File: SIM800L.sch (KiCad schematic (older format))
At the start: 9 parts, among them P3 CONN_01X06, P4 CONN_01X06, Q1 BC849

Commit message: Modifico algunos componentes. Seteo algunos encapsulados. Ordeno los componentes en el PCB.
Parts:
- D5: footprint (none) -> LEDs:LED_1206
- D6, D7: footprint (none) -> Diodes_SMD:SOD-123
- P3, P4: footprint (none) -> Pin_Headers:Pin_Header_Angled_1x06
- Q1: footprint SOT-23 -> TO_SOT_Packages_SMD:SOT-23
- R2, R3, R4: footprint (none) -> SMD_Packages:SMD-1206_Pol
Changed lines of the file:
@@
 EESchema Schematic File Version 2
 LIBS:tp_vino-cache
+LIBS:74xgxx
+LIBS:74xx
+LIBS:Altera
+LIBS:ESD_Protection
+LIBS:Lattice
+LIBS:Oscillators
+LIBS:Power_Management
+LIBS:Worldsemi
+LIBS:Xicor
+LIBS:Zilog
+LIBS:ac-dc
+LIBS:actel
+LIBS:adc-dac
+LIBS:analog_devices
+LIBS:analog_switches
+LIBS:atmel
+LIBS:audio
+LIBS:brooktre
+LIBS:cmos4000
+LIBS:cmos_ieee
+LIBS:conn
+LIBS:contrib
+LIBS:cypress
+LIBS:dc-dc
+LIBS:device
+LIBS:digital-audio
+LIBS:diode
+LIBS:display
+LIBS:dsp
+LIBS:elec-unifil
+LIBS:ftdi
+LIBS:gennum
+LIBS:graphic
+LIBS:hc11
+LIBS:intel
+LIBS:interface
+LIBS:ir
+LIBS:linear
+LIBS:logo
+LIBS:maxim
+LIBS:memory
+LIBS:microchip
+LIBS:microchip_dspic33dsc
+LIBS:microchip_pic10mcu
+LIBS:microchip_pic12mcu
+LIBS:microchip_pic16mcu
+LIBS:microchip_pic18mcu
+LIBS:microchip_pic32mcu
+LIBS:microcontrollers
+LIBS:motor_drivers
+LIBS:motorola
+LIBS:msp430
+LIBS:nordicsemi
+LIBS:nxp_armmcu
+LIBS:onsemi
+LIBS:opto
+LIBS:philips
+LIBS:power
+LIBS:powerint
+LIBS:pspice
+LIBS:references
+LIBS:regul
+LIBS:relays
+LIBS:rfcom
+LIBS:sensors
+LIBS:silabs
+LIBS:siliconi
+LIBS:stm8
+LIBS:stm32
+LIBS:supertex
+LIBS:switches
+LIBS:texas
+LIBS:transf
+LIBS:transistors
+LIBS:ttl_ieee
+LIBS:valves
+LIBS:video
+LIBS:xilinx
 EELAYER 25 0
 EELAYER END
@@
 F 0 "P3" H 3350 4550 50  0000 C CNN
 F 1 "CONN_01X06" V 3450 4200 50  0000 C CNN
-F 2 "" H 3350 4200 50  0000 C CNN
+F 2 "Pin_Headers:Pin_Header_Angled_1x06" H 3350 4200 50  0001 C CNN
 F 3 "" H 3350 4200 50  0000 C CNN
 	1    3350 4200
@@
 F 0 "P4" H 3850 4550 50  0000 C CNN
 F 1 "CONN_01X06" V 3950 4200 50  0000 C CNN
-F 2 "" H 3850 4200 50  0000 C CNN
+F 2 "Pin_Headers:Pin_Header_Angled_1x06" H 3850 4200 50  0001 C CNN
 F 3 "" H 3850 4200 50  0000 C CNN
 	1    3850 4200
@@
 $EndComp
 $Comp
-L GND #PWR029
+L GND #PWR025
 U 1 1 581A0E24
 P 4150 4500
-F 0 "#PWR029" H 4150 4250 50  0001 C CNN
+F 0 "#PWR025" H 4150 4250 50  0001 C CNN
 F 1 "GND" H 4150 4350 50  0000 C CNN
 F 2 "" H 4150 4500 50  0000 C CNN
@@
 F 0 "R2" V 4530 3500 50  0000 C CNN
 F 1 "R" V 4450 3500 50  0000 C CNN
-F 2 "" V 4380 3500 50  0000 C CNN
+F 2 "SMD_Packages:SMD-1206_Pol" V 4380 3500 50  0001 C CNN
 F 3 "" H 4450 3500 50  0000 C CNN
 	1    4450 3500
@@
 F 0 "R3" V 5180 3500 50  0000 C CNN
 F 1 "R" V 5100 3500 50  0000 C CNN
-F 2 "" V 5030 3500 50  0000 C CNN
+F 2 "SMD_Packages:SMD-1206_Pol" V 5030 3500 50  0001 C CNN
 F 3 "" H 5100 3500 50  0000 C CNN
 	1    5100 3500
@@
 F 0 "Q1" H 5500 3225 50  0000 L CNN
 F 1 "BC849" H 5500 3150 50  0000 L CNN
-F 2 "SOT-23" H 5500 3075 50  0000 L CIN
+F 2 "TO_SOT_Packages_SMD:SOT-23" H 5500 3075 50  0000 L CIN
 F 3 "" H 5300 3150 50  0000 L CNN
 	1    5300 3150
@@
 $EndComp
 $Comp
-L GND #PWR030
+L GND #PWR026
 U 1 1 581A0E28
 P 5400 3550
-F 0 "#PWR030" H 5400 3300 50  0001 C CNN
+F 0 "#PWR026" H 5400 3300 50  0001 C CNN
 F 1 "GND" H 5400 3400 50  0000 C CNN
 F 2 "" H 5400 3550 50  0000 C CNN
@@
 F 0 "R4" V 5480 2550 50  0000 C CNN
 F 1 "R" V 5400 2550 50  0000 C CNN
-F 2 "" V 5330 2550 50  0000 C CNN
+F 2 "SMD_Packages:SMD-1206_Pol" V 5330 2550 50  0001 C CNN
 F 3 "" H 5400 2550 50  0000 C CNN
 	1    5400 2550
@@
 F 0 "D5" H 5700 2400 50  0000 C CNN
 F 1 "LED" H 5700 2200 50  0000 C CNN
-F 2 "" H 5700 2300 50  0000 C CNN
+F 2 "LEDs:LED_1206" H 5700 2300 50  0001 C CNN
 F 3 "" H 5700 2300 50  0000 C CNN
 	1    5700 2300
@@
 NoConn ~ 3150 3950
 $Comp
-L +5V #PWR031
+L +5V #PWR027
 U 1 1 581A0E2B
 P 6000 2250
-F 0 "#PWR031" H 6000 2100 50  0001 C CNN
+F 0 "#PWR027" H 6000 2100 50  0001 C CNN
 F 1 "+5V" H 6000 2390 50  0000 C CNN
 F 2 "" H 6000 2250 50  0000 C CNN
@@
 F 0 "D6" H 5800 4400 50  0000 C CNN
 F 1 "ZENER_4,3V_1N4731" V 6000 4700 50  0000 C CNN
-F 2 "" H 5800 4300 50  0000 C CNN
+F 2 "Diodes_SMD:SOD-123" H 5800 4300 50  0001 C CNN
 F 3 "" H 5800 4300 50  0000 C CNN
 	1    5800 4300
@@
 $EndComp
 $Comp
-L GND #PWR032
+L GND #PWR028
 U 1 1 581A0E2D
 P 5800 4550
-F 0 "#PWR032" H 5800 4300 50  0001 C CNN
+F 0 "#PWR028" H 5800 4300 50  0001 C CNN
 F 1 "GND" H 5800 4400 50  0000 C CNN
 F 2 "" H 5800 4550 50  0000 C CNN
@@
 F 0 "D7" H 6300 4150 40  0000 C CNN
 F 1 "DIODE_1N4007" H 6300 3950 40  0000 C CNN
-F 2 "" H 6300 4050 60  0000 C CNN
+F 2 "Diodes_SMD:SOD-123" H 6300 4050 60  0001 C CNN
 F 3 "" H 6300 4050 60  0000 C CNN
 	1    6300 4050
@@
 $EndComp
 $Comp
-L +5V #PWR033
+L +5V #PWR029
 U 1 1 581A0E2F
 P 6600 3750
-F 0 "#PWR033" H 6600 3600 50  0001 C CNN
+F 0 "#PWR029" H 6600 3600 50  0001 C CNN
 F 1 "+5V" H 6600 3890 50  0000 C CNN
 F 2 "" H 6600 3750 50  0000 C CNN

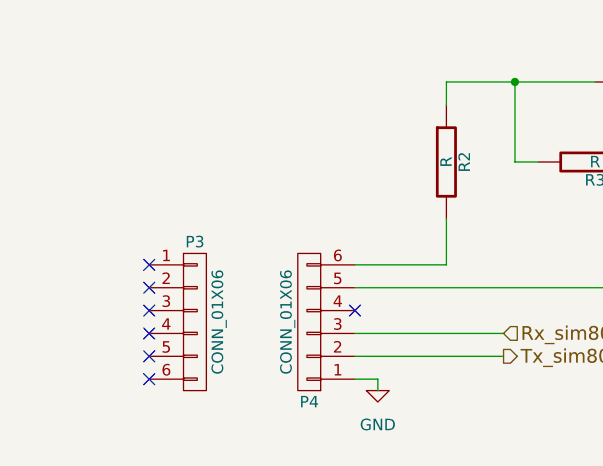
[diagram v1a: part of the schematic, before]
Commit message: Algunas modificaciones en el circuito  oreno el pcb.
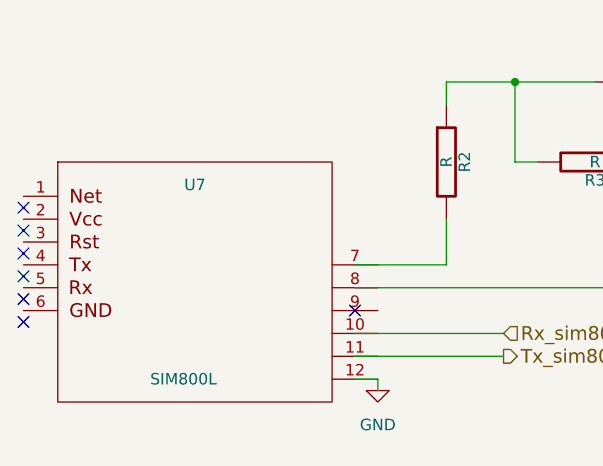
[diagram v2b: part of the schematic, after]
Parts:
- removed P3, P4: CONN_01X06, Pin_Headers:Pin_Header_Angled_1x06, symbol CONN_01X06
- added U7: SIM800L, symbol SIM800L
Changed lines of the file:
@@
 LIBS:video
 LIBS:xilinx
+LIBS:sim800l
 EELAYER 25 0
 EELAYER END
@@
 Fuente de alimentación con rango aproximado de entrada de 12 a 30V (CC).\nTensiones de salida: 5V, 3A y 3.3V, 1A.\nPosibilidad de alimentar la CIAA a través del puerto USB mediante la conexión con D1.
 $Comp
-L CONN_01X06 P3
-U 1 1 581A0E22
-P 3350 4200
-F 0 "P3" H 3350 4550 50  0000 C CNN
-F 1 "CONN_01X06" V 3450 4200 50  0000 C CNN
-F 2 "Pin_Headers:Pin_Header_Angled_1x06" H 3350 4200 50  0001 C CNN
-F 3 "" H 3350 4200 50  0000 C CNN
-	1    3350 4200
-	1    0    0    -1
-$EndComp
-$Comp
-L CONN_01X06 P4
-U 1 1 581A0E23
-P 3850 4200
-F 0 "P4" H 3850 4550 50  0000 C CNN
-F 1 "CONN_01X06" V 3950 4200 50  0000 C CNN
-F 2 "Pin_Headers:Pin_Header_Angled_1x06" H 3850 4200 50  0001 C CNN
-F 3 "" H 3850 4200 50  0000 C CNN
-	1    3850 4200
-	-1   0    0    1
-$EndComp
-$Comp
-L GND #PWR025
+L GND #PWR020
 U 1 1 581A0E24
 P 4150 4500
-F 0 "#PWR025" H 4150 4250 50  0001 C CNN
+F 0 "#PWR020" H 4150 4250 50  0001 C CNN
 F 1 "GND" H 4150 4350 50  0000 C CNN
 F 2 "" H 4150 4500 50  0000 C CNN
@@
 $EndComp
 $Comp
-L GND #PWR026
+L GND #PWR021
 U 1 1 581A0E28
 P 5400 3550
-F 0 "#PWR026" H 5400 3300 50  0001 C CNN
+F 0 "#PWR021" H 5400 3300 50  0001 C CNN
 F 1 "GND" H 5400 3400 50  0000 C CNN
 F 2 "" H 5400 3550 50  0000 C CNN
@@
 	1    0    0    -1
 $EndComp
-NoConn ~ 3150 4450
-NoConn ~ 3150 4350
-NoConn ~ 3150 4250
-NoConn ~ 3150 4150
-NoConn ~ 3150 4050
-NoConn ~ 3150 3950
-$Comp
-L +5V #PWR027
+NoConn ~ 2600 4200
+NoConn ~ 2600 4100
+NoConn ~ 2600 4000
+NoConn ~ 2600 3900
+NoConn ~ 2600 3800
+NoConn ~ 2600 3700
+$Comp
+L +5V #PWR022
 U 1 1 581A0E2B
 P 6000 2250
-F 0 "#PWR027" H 6000 2100 50  0001 C CNN
+F 0 "#PWR022" H 6000 2100 50  0001 C CNN
 F 1 "+5V" H 6000 2390 50  0000 C CNN
 F 2 "" H 6000 2250 50  0000 C CNN
@@
 $EndComp
 $Comp
-L GND #PWR028
+L GND #PWR023
 U 1 1 581A0E2D
 P 5800 4550
-F 0 "#PWR028" H 5800 4300 50  0001 C CNN
+F 0 "#PWR023" H 5800 4300 50  0001 C CNN
 F 1 "GND" H 5800 4400 50  0000 C CNN
 F 2 "" H 5800 4550 50  0000 C CNN
@@
 $EndComp
 $Comp
-L +5V #PWR029
+L +5V #PWR024
 U 1 1 581A0E2F
 P 6600 3750
-F 0 "#PWR029" H 6600 3600 50  0001 C CNN
+F 0 "#PWR024" H 6600 3600 50  0001 C CNN
 F 1 "+5V" H 6600 3890 50  0000 C CNN
 F 2 "" H 6600 3750 50  0000 C CNN
@@
 Wire Wire Line
 	5500 2300 5400 2300
+$Comp
+L SIM800L U7
+U 1 1 581BDB88
+P 3450 4000
+F 0 "U7" H 3350 4400 50  0000 C CNN
+F 1 "SIM800L" H 3300 3550 50  0000 C CNN
+F 2 "" H 2800 4050 50  0000 C CNN
+F 3 "" H 2800 4050 50  0000 C CNN
+	1    3450 4000
+	1    0    0    -1
+$EndComp
 $EndSCHEMATC

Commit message: Add digikey code and comment schematic.
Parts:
- D5: Digikey# (none) -> SML-LX1206GC-TR SML-LX1206GC-TR
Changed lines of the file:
@@
 F 2 "LEDs:LED_1206" H 5700 2300 50  0001 C CNN
 F 3 "" H 5700 2300 50  0000 C CNN
+F 4 "SML-LX1206GC-TR	SML-LX1206GC-TR" H 4200 1450 60  0001 C CNN "Digikey#"
 	1    5700 2300
 	1    0    0    -1
